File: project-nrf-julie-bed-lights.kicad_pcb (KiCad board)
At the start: 2 copper layers, 34 parts, among them J1 PJ-036AH-SMT-TR, J2 Screw_Terminal_01x04, J3 Left, J4 Right, Q1 Si231BDS, Q2 Si231BDS, Q3 Si231BDS, Q4 RU1J002YN, Q5 RU1J002YN, Q6 PJA3441_R1_00001, SW1 PEC11S-9213K-S0015, U1 AP63300WU-7

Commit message: Update board
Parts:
- added R10: 10k, Resistor_SMD:R_0603_1608Metric, F.Cu at (114.0, -50.0)
- added R11: 10k, Resistor_SMD:R_0603_1608Metric, F.Cu at (110.0, -50.0)
- S1: value B3FS-1012 -> Change mode
- SW1: value PEC11S-9213K-S0015 -> Change value
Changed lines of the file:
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@@
+    )
+  )
+  (footprint "Resistor_SMD:R_0603_1608Metric" (layer "F.Cu")
+    (at 109.99 -50)
+    (descr "Resistor SMD 0603 (1608 Metric), square (rectangular) end terminal, IPC_7351 nominal, (Body size source: IPC-SM-782 page 72, https://www.pcb-3d.com/wordpress/wp-content/uploads/ipc-sm-782a_amendment_1_and_2.pdf), generated with kicad-footprint-generator")
+    (tags "resistor")
+    (property "Sheetfile" "project-nrf-julie-bed-lights.kicad_sch")
+    (property "Sheetname" "")
+    (attr smd)
+    (fp_text reference "R11" (at 0 -1.43) (layer "F.SilkS") hide
+      (effects (font (size 1 1) (thickness 0.15)))
+    )
+    (fp_text value "10k" (at 0 1.43) (layer "F.Fab")
+      (effects (font (size 1 1) (thickness 0.15)))
+    )
+    (fp_text user "${REFERENCE}" (at 0 0) (layer "F.Fab")
+      (effects (font (size 0.4 0.4) (thickness 0.06)))
+    )
+    (fp_line (start -0.237258 0.5225) (end 0.237258 0.5225) (layer "F.SilkS") (width 0.12))
+    (fp_line (start -0.237258 -0.5225) (end 0.237258 -0.5225) (layer "F.SilkS") (width 0.12))
+    (fp_line (start 1.48 0.73) (end -1.48 0.73) (layer "F.CrtYd") (width 0.05))
+    (fp_line (start 1.48 -0.73) (end 1.48 0.73) (layer "F.CrtYd") (width 0.05))
+    (fp_line (start -1.48 -0.73) (end 1.48 -0.73) (layer "F.CrtYd") (width 0.05))
+    (fp_line (start -1.48 0.73) (end -1.48 -0.73) (layer "F.CrtYd") (width 0.05))
+    (fp_line (start -0.8 -0.4125) (end 0.8 -0.4125) (layer "F.Fab") (width 0.1))
+    (fp_line (start 0.8 0.4125) (end -0.8 0.4125) (layer "F.Fab") (width 0.1))
+    (fp_line (start 0.8 -0.4125) (end 0.8 0.4125) (layer "F.Fab") (width 0.1))
+    (fp_line (start -0.8 0.4125) (end -0.8 -0.4125) (layer "F.Fab") (width 0.1))
+    (pad "1" smd roundrect (at -0.825 0) (size 0.8 0.95) (layers "F.Cu" "F.Paste" "F.Mask") (roundrect_rratio 0.25)
+      (net 3 "+3V0") (pintype "passive"))
+    (pad "2" smd roundrect (at 0.825 0) (size 0.8 0.95) (layers "F.Cu" "F.Paste" "F.Mask") (roundrect_rratio 0.25)
+      (net 32 "/PhaseA") (pintype "passive"))
+    (model "${KICAD6_3DMODEL_DIR}/Resistor_SMD.3dshapes/R_0603_1608Metric.wrl"
+      (offset (xyz 0 0 0))
+      (scale (xyz 1 1 1))
+      (rotate (xyz 0 0 0))
     )
   )
@@
       (net 8 "Net-(D1-Pad2)") (pinfunction "A") (pintype "passive"))
     (model "${KICAD6_3DMODEL_DIR}/LED_SMD.3dshapes/LED_0603_1608Metric.wrl"
+      (offset (xyz 0 0 0))
+      (scale (xyz 1 1 1))
+      (rotate (xyz 0 0 0))
+    )
+  )
+  (footprint "Resistor_SMD:R_0603_1608Metric" (layer "F.Cu")
+    (at 114 -50)
+    (descr "Resistor SMD 0603 (1608 Metric), square (rectangular) end terminal, IPC_7351 nominal, (Body size source: IPC-SM-782 page 72, https://www.pcb-3d.com/wordpress/wp-content/uploads/ipc-sm-782a_amendment_1_and_2.pdf), generated with kicad-footprint-generator")
+    (tags "resistor")
+    (property "Sheetfile" "project-nrf-julie-bed-lights.kicad_sch")
+    (property "Sheetname" "")
+    (attr smd)
+    (fp_text reference "R10" (at 0 -1.43) (layer "F.SilkS") hide
+      (effects (font (size 1 1) (thickness 0.15)))
+    )
+    (fp_text value "10k" (at 0 1.43) (layer "F.Fab")
+      (effects (font (size 1 1) (thickness 0.15)))
+    )
+    (fp_text user "${REFERENCE}" (at 0 0) (layer "F.Fab")
+      (effects (font (size 0.4 0.4) (thickness 0.06)))
+    )
+    (fp_line (start -0.237258 0.5225) (end 0.237258 0.5225) (layer "F.SilkS") (width 0.12))
+    (fp_line (start -0.237258 -0.5225) (end 0.237258 -0.5225) (layer "F.SilkS") (width 0.12))
+    (fp_line (start -1.48 0.73) (end -1.48 -0.73) (layer "F.CrtYd") (width 0.05))
+    (fp_line (start 1.48 -0.73) (end 1.48 0.73) (layer "F.CrtYd") (width 0.05))
+    (fp_line (start -1.48 -0.73) (end 1.48 -0.73) (layer "F.CrtYd") (width 0.05))
+    (fp_line (start 1.48 0.73) (end -1.48 0.73) (layer "F.CrtYd") (width 0.05))
+    (fp_line (start 0.8 -0.4125) (end 0.8 0.4125) (layer "F.Fab") (width 0.1))
+    (fp_line (start -0.8 0.4125) (end -0.8 -0.4125) (layer "F.Fab") (width 0.1))
+    (fp_line (start 0.8 0.4125) (end -0.8 0.4125) (layer "F.Fab") (width 0.1))
+    (fp_line (start -0.8 -0.4125) (end 0.8 -0.4125) (layer "F.Fab") (width 0.1))
+    (pad "1" smd roundrect (at -0.825 0) (size 0.8 0.95) (layers "F.Cu" "F.Paste" "F.Mask") (roundrect_rratio 0.25)
+      (net 3 "+3V0") (pintype "passive"))
+    (pad "2" smd roundrect (at 0.825 0) (size 0.8 0.95) (layers "F.Cu" "F.Paste" "F.Mask") (roundrect_rratio 0.25)
+      (net 33 "/PhaseB") (pintype "passive"))
+    (model "${KICAD6_3DMODEL_DIR}/Resistor_SMD.3dshapes/R_0603_1608Metric.wrl"
       (offset (xyz 0 0 0))
       (scale (xyz 1 1 1))
@@
       (effects (font (size 1 1) (thickness 0.15)))
     )
-    (fp_text value "B3FS-1012" (at 0 4.5) (layer "F.Fab")
+    (fp_text value "Change mode" (at 0 4.5) (layer "F.Fab")
       (effects (font (size 1 1) (thickness 0.15)))
     )
@@
       (effects (font (size 1 1) (thickness 0.15)))
     )
-    (fp_text value "PEC11S-9213K-S0015" (at 0 12 -90 unlocked) (layer "F.Fab")
-      (effects (font (size 1 1) (thickness 0.15)))
-    )
+    (fp_text value "Change value" (at 0 12 -90 unlocked) (layer "F.Fab")
+      (effects (font (size 1 1) (thickness 0.15)))
+    )

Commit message: About half placement
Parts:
- moved Q1 110.2 mm to (196.0, 40.0)
- moved R10 103.2 mm to (78.8, 47.0)
- moved R11 103.0 mm to (75.3, 47.0)
- moved Q3 102.3 mm to (175.5, 40.5)
- moved R5 95.2 mm to (175.0, 34.5)
- moved S1 93.2 mm to (96.0, 30.0), turned to 90 degrees
- moved R3 92.9 mm to (196.2, 33.5)
- moved R4 87.2 mm to (158.5, 34.5)
- moved SW1 79.6 mm to (77.0, 35.0), turned to 0 degrees
- moved Q5 54.1 mm to (212.0, -29.5)
- moved D2 51.4 mm to (211.8, -17.5)
- moved R6 48.8 mm to (177.0, -2.00)
- moved Q2 45.0 mm to (158.9, 40.0)
- moved Q4 40.0 mm to (183.5, -12.0)
- moved R8 39.4 mm to (210.5, -35.0)
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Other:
- board outline added: 89 x 58 mm

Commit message: Everything placed except step-down
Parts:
- moved R8 136.4 mm to (100.0, 45.0)
- moved Q5 135.9 mm to (100.0, 47.5)
- moved R9 127.1 mm to (103.5, 45.0)
- moved Q6 124.7 mm to (81.5, 58.5), turned to 180 degrees
- moved D3 119.9 mm to (83.0, 62.5), turned to 180 degrees
- moved D2 118.5 mm to (110.8, 44.4), turned to 180 degrees
- moved C1 108.0 mm to (51.0, 97.5)
- moved C2 108.0 mm to (64.0, 94.0)
- moved C3 108.0 mm to (58.0, 98.0)
- moved C4 108.0 mm to (67.5, 89.0)
- moved L1 108.0 mm to (60.0, 89.0)
- moved R1 108.0 mm to (46.5, 87.5)
- moved R2 108.0 mm to (46.0, 92.5)
- moved U1 108.0 mm to (54.5, 90.5)
- moved R3 103.0 mm to (99.0, 67.5), turned to -90 degrees
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
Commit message: First complete placement done
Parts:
- moved R7 57.4 mm to (47.0, 29.5)
- moved R9 57.2 mm to (47.0, 36.0)
- moved R6 56.5 mm to (44.0, 32.0), turned to -90 degrees
- moved R8 56.4 mm to (44.0, 38.5), turned to -90 degrees
- moved Q4 53.9 mm to (47.0, 32.0)
- moved Q5 53.8 mm to (47.0, 38.5)
- moved C2 33.4 mm to (45.0, 66.5)
- moved C1 29.6 mm to (49.0, 68.0), turned to 180 degrees
- moved C3 28.6 mm to (46.0, 72.0), turned to -90 degrees
- moved L1 25.3 mm to (44.5, 69.0), turned to 180 degrees
- moved D2 24.4 mm to (92.1, 28.6)
- moved C4 22.9 mm to (49.0, 75.5)
- moved D1 22.7 mm to (92.1, 26.0)
- moved U1 20.3 mm to (49.0, 71.0), turned to 180 degrees
- moved R2 18.6 mm to (51.5, 74.7), turned to 90 degrees
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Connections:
- J4 pad 11: /Vert_PWM -> /Bleu_PWM
- J4 pad 9: /Bleu_PWM -> /Vert_PWM
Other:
- board size 89 x 58 mm -> 76 x 58 mm
- board text added: "Color"
- board text added: "Intensity"

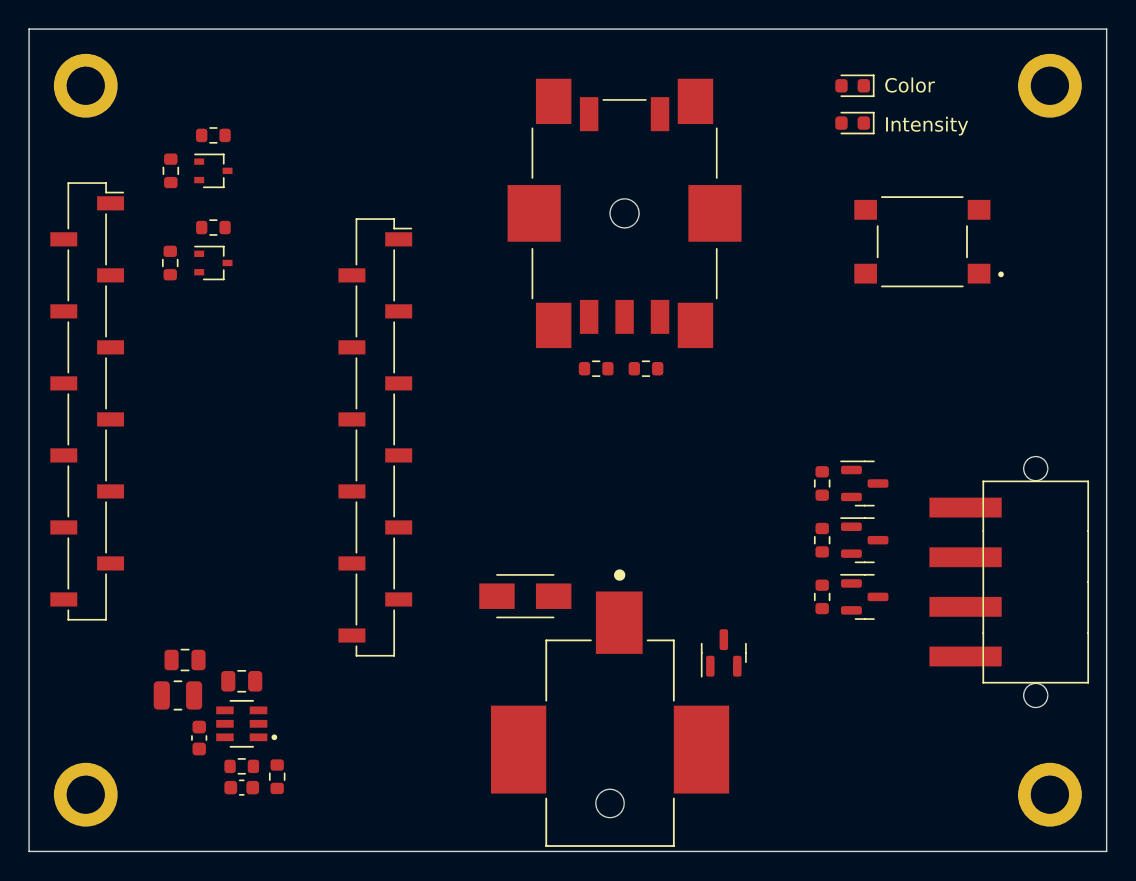
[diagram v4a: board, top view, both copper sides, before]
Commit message: Routing except power done
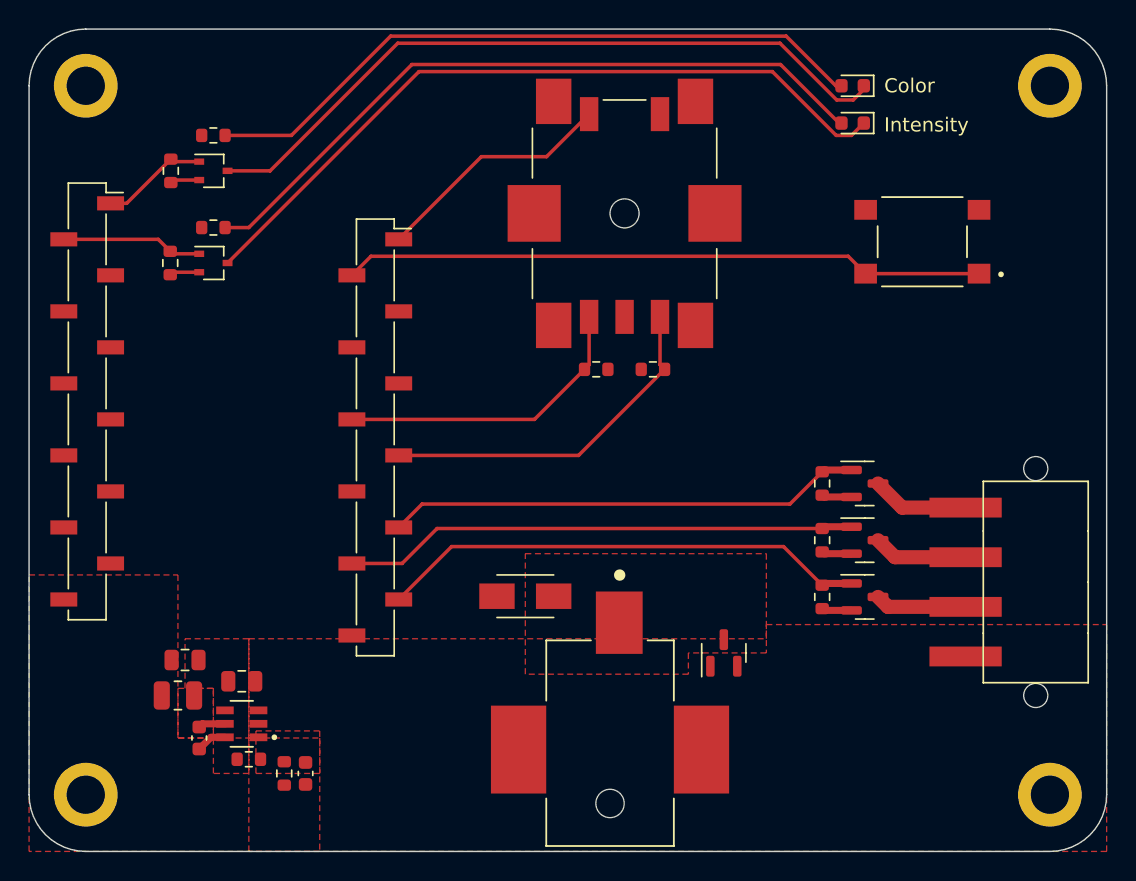
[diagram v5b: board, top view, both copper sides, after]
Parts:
- moved C4 4.61 mm to (53.5, 74.5), turned to 90 degrees
- moved R1 3.04 mm to (52.0, 74.5), turned to 90 degrees
- moved R2 2.35 mm to (49.5, 73.5), turned to 180 degrees
- moved R10 0.49 mm to (78.0, 46.0)
- turned R11 to 180 degrees
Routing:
- net Net-(D2-Pad1): track 0.00 -> 52.7 mm
- net Net-(D1-Pad1): track 0.00 -> 50.8 mm
- net Net-(D2-Pad2): track 0.00 -> 49.9 mm
- net Net-(D1-Pad2): track 0.00 -> 47.8 mm
- net /External_Button: track 0.00 -> 45.3 mm
- net /Rouge_PWM: track 0.00 -> 36.3 mm
- net /Bleu_PWM: track 0.00 -> 34.7 mm
- net /Vert_PWM: track 0.00 -> 33.6 mm
- net /PhaseB: track 0.00 -> 25.1 mm
- net /PhaseA: track 0.00 -> 21.7 mm
- net /Encoder_Button: track 0.00 -> 17.1 mm
- net GND: track 0.00 -> 10.5 mm
- net /Intensity_LED: track 0.00 -> 9.97 mm
- net /Color_LED: track 0.00 -> 7.61 mm
- net /Vert: track 0.00 -> 6.88 mm
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- added copper zone on F.Cu, net +12V
- added copper zone on F.Cu, net +3V0
- added copper zone on F.Cu, net GND
- added copper zone on F.Cu, net Net-(C3-Pad1)
- added copper zone on F.Cu, net Net-(C4-Pad2)
- added copper zone on F.Cu, net VCC
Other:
- outline, holes or cut-outs redrawn
